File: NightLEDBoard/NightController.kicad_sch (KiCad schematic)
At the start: 10 parts

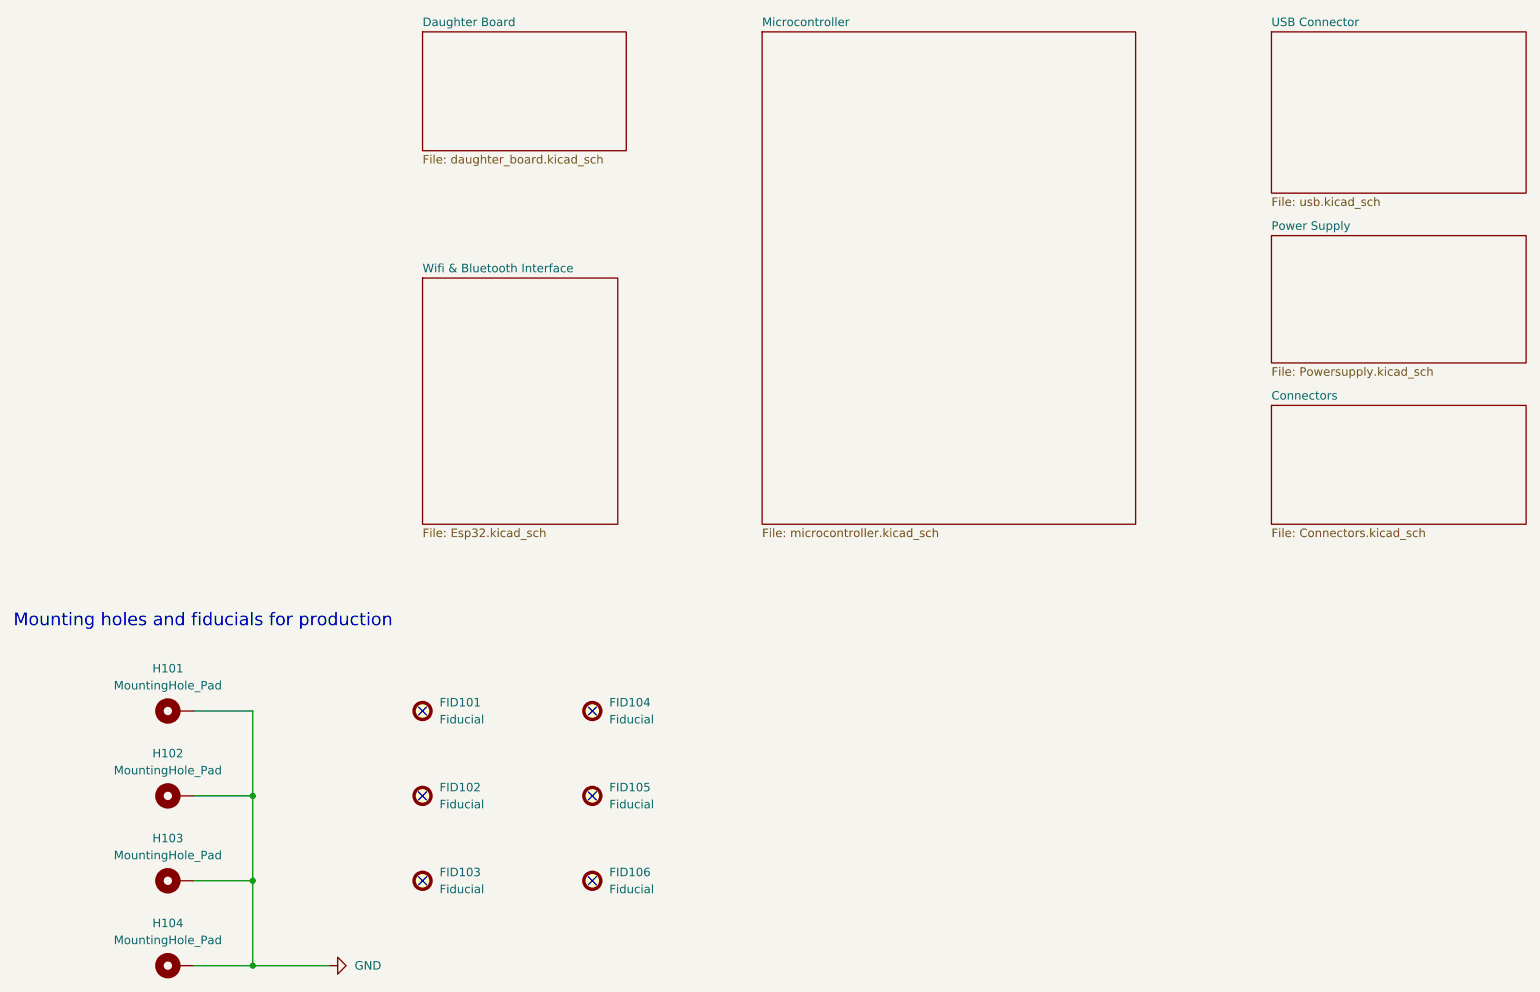
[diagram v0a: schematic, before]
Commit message: Add second pcb
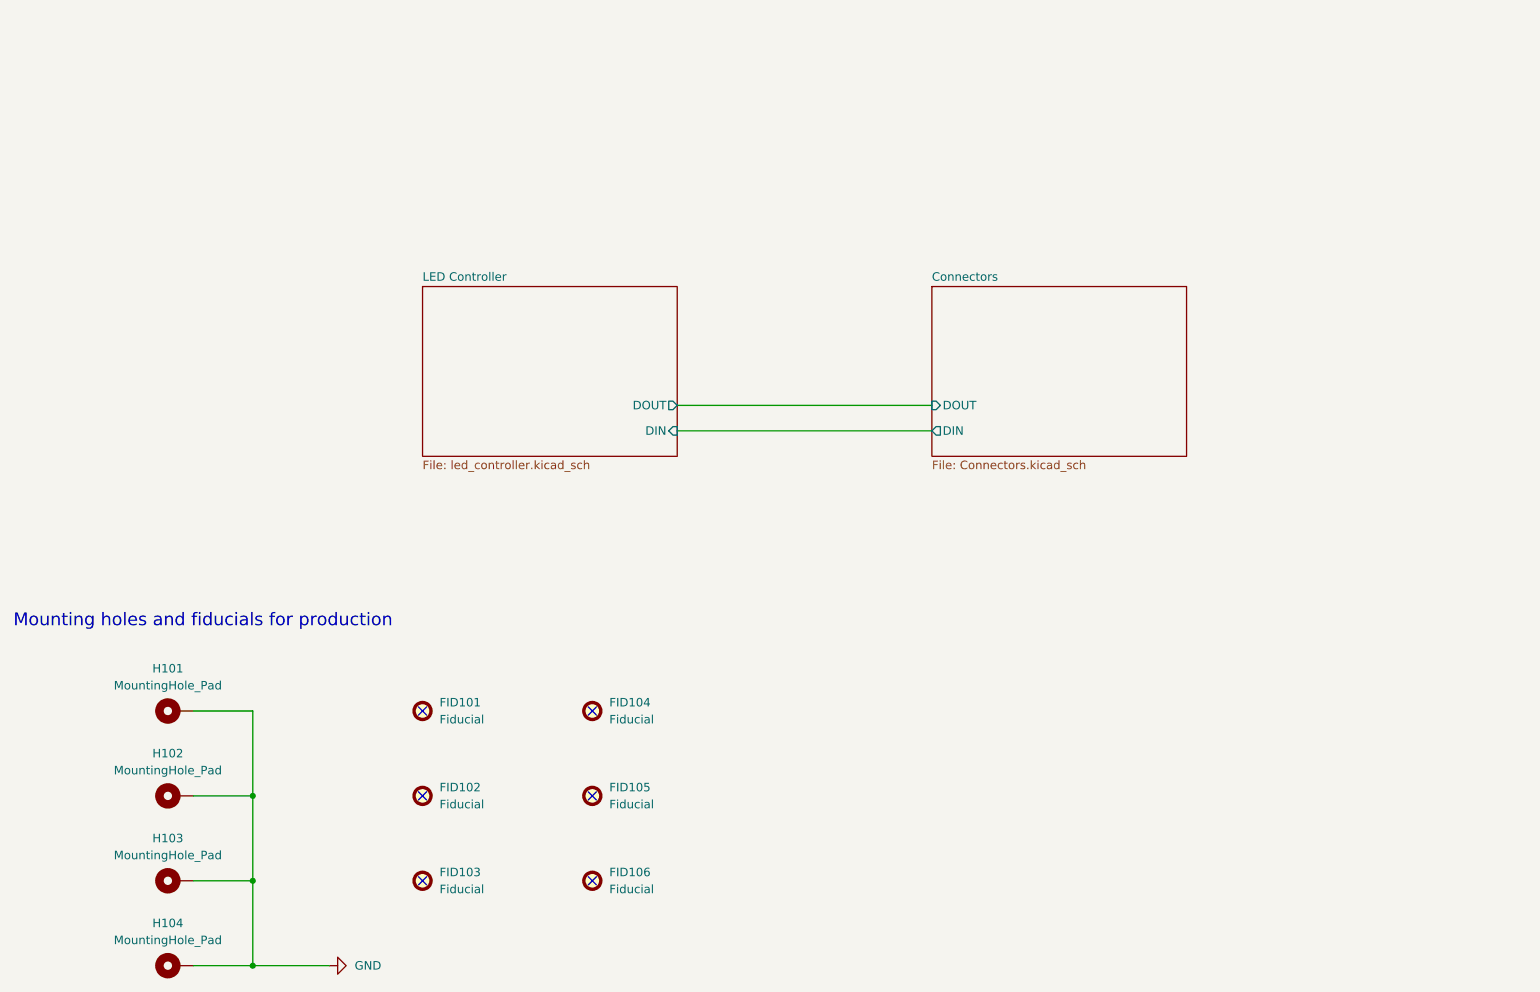
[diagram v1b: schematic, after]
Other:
- removed sheet Daughter Board
- removed sheet Microcontroller
- removed sheet Power Supply
- removed sheet USB Connector
- removed sheet Wifi & Bluetooth Interface
- added sheet LED Controller (led_controller.kicad_sch)
- sheet Connectors ports: added DIN, DOUT; removed none
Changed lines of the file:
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@@
 	(generator "eeschema")
 	(generator_version "8.0")
-	(paper "A3")
+	(paper "A4")
 	(title_block
 		(title "NightLight")
@@
 	(wire
 		(pts
+			(xy 114.3 110.49) (xy 152.4 110.49)
+		)
+		(stroke
+			(width 0)
+			(type default)
+		)
+	)
+	(wire
+		(pts
 			(xy 50.8 190.5) (xy 62.23 190.5)
 		)
@@
 		(pts
 			(xy 50.8 190.5) (xy 41.91 190.5)
+		)
+		(stroke
+			(width 0)
+			(type default)
+		)
+	)
+	(wire
+		(pts
+			(xy 114.3 106.68) (xy 152.4 106.68)
 		)
 		(stroke
@@
 	)
 	(sheet
-		(at 76.2 87.63)
-		(size 29.21 36.83)
+		(at 152.4 88.9)
+		(size 38.1 25.4)
 		(fields_autoplaced yes)
 		(stroke
@@
 			(color 0 0 0 0.0000)
 		)
-		(property "Sheetname" "Wifi & Bluetooth Interface"
-			(at 76.2 86.9184 0)
+		(property "Sheetname" "Connectors"
+			(at 152.4 88.1884 0)
 			(effects
 				(font
@@
 			)
 		)
-		(property "Sheetfile" "Esp32.kicad_sch"
-			(at 76.2 125.0446 0)
+		(property "Sheetfile" "Connectors.kicad_sch"
+			(at 152.4 114.8846 0)
 			(effects
 				(font
@@
 			)
 		)
-		(instances
-			(project "NightController"
-				(path "/84972824-c6a3-4762-8148-c4d5b5ede147"
-					(page "4")
+		(pin "DOUT" input
+			(at 152.4 106.68 180)
+			(effects
+				(font
+					(size 1.27 1.27)
+				)
+				(justify left)
+			)
+		)
+		(pin "DIN" output
+			(at 152.4 110.49 180)
+			(effects
+				(font
+					(size 1.27 1.27)
+				)
+				(justify left)
+			)
+		)
+		(instances
+			(project "NightController"
+				(path "/84972824-c6a3-4762-8148-c4d5b5ede147"
+					(page "2")
 				)
 			)
@@
 	)
 	(sheet
-		(at 76.2 50.8)
-		(size 30.48 17.78)
+		(at 76.2 88.9)
+		(size 38.1 25.4)
 		(fields_autoplaced yes)
 		(stroke
@@
 			(color 0 0 0 0.0000)
 		)
-		(property "Sheetname" "Daughter Board"
-			(at 76.2 50.0884 0)
+		(property "Sheetname" "LED Controller"
+			(at 76.2 88.1884 0)
 			(effects
 				(font
@@
 			)
 		)
-		(property "Sheetfile" "daughter_board.kicad_sch"
-			(at 76.2 69.1646 0)
+		(property "Sheetfile" "led_controller.kicad_sch"
+			(at 76.2 114.8846 0)
 			(effects
 				(font
@@
 			)
 		)
+		(pin "DIN" input
+			(at 114.3 110.49 0)
+			(effects
+				(font
+					(size 1.27 1.27)
+				)
+				(justify right)
+			)
+		)
+		(pin "DOUT" output
+			(at 114.3 106.68 0)
+			(effects
+				(font
+					(size 1.27 1.27)
+				)
+				(justify right)
+			)
+		)
 		(instances
 			(project "NightController"
@@
 				)
 			)
-		)
-	)
-	(sheet
-		(at 203.2 81.28)
-		(size 38.1 19.05)
-		(fields_autoplaced yes)
-		(stroke
-			(width 0.1524)
-			(type solid)
-		)
-		(fill
-			(color 0 0 0 0.0000)
-		)
-		(property "Sheetname" "Power Supply"
-			(at 203.2 80.5684 0)
-			(effects
-				(font
-					(size 1.27 1.27)
-				)
-				(justify left bottom)
-			)
-		)
-		(property "Sheetfile" "Powersupply.kicad_sch"
-			(at 203.2 100.9146 0)
-			(effects
-				(font
-					(size 1.27 1.27)
-				)
-				(justify left top)
-			)
-		)
-		(instances
-			(project "NightController"
-				(path "/84972824-c6a3-4762-8148-c4d5b5ede147"
-					(page "6")
-				)
-			)
-		)
-	)
-	(sheet
-		(at 203.2 106.68)
-		(size 38.1 17.78)
-		(fields_autoplaced yes)
-		(stroke
-			(width 0.1524)
-			(type solid)
-		)
-		(fill
-			(color 0 0 0 0.0000)
-		)
-		(property "Sheetname" "Connectors"
-			(at 203.2 105.9684 0)
-			(effects
-				(font
-					(size 1.27 1.27)
-				)
-				(justify left bottom)
-			)
-		)
-		(property "Sheetfile" "Connectors.kicad_sch"
-			(at 203.2 125.0446 0)
-			(effects
-				(font
-					(size 1.27 1.27)
-				)
-				(justify left top)
-			)
-		)
-		(instances
-			(project "NightController"
-				(path "/84972824-c6a3-4762-8148-c4d5b5ede147"
-					(page "7")
-				)
-			)
-		)
-	)
-	(sheet
-		(at 127 50.8)
-		(size 55.88 73.66)
-		(fields_autoplaced yes)
-		(stroke
-			(width 0.1524)
-			(type solid)
-		)
-		(fill
-			(color 0 0 0 0.0000)
-		)
-		(property "Sheetname" "Microcontroller"
-			(at 127 50.0884 0)
-			(effects
-				(font
-					(size 1.27 1.27)
-				)
-				(justify left bottom)
-			)
-		)
-		(property "Sheetfile" "microcontroller.kicad_sch"
-			(at 127 125.0446 0)
-			(effects
-				(font
-					(size 1.27 1.27)
-				)
-				(justify left top)
-			)
-		)
-		(instances
-			(project "NightController"
-				(path "/84972824-c6a3-4762-8148-c4d5b5ede147"
-					(page "2")
-				)
-			)
-		)
-	)
-	(sheet
-		(at 203.2 50.8)
-		(size 38.1 24.13)
-		(fields_autoplaced yes)
-		(stroke
-			(width 0.1524)
-			(type solid)
-		)
-		(fill
-			(color 0 0 0 0.0000)
-		)
-		(property "Sheetname" "USB Connector"
-			(at 203.2 50.0884 0)
-			(effects
-				(font
-					(size 1.27 1.27)
-				)
-				(justify left bottom)
-			)
-		)
-		(property "Sheetfile" "usb.kicad_sch"
-			(at 203.2 75.5146 0)
-			(effects
-				(font
-					(size 1.27 1.27)
-				)
-				(justify left top)
-			)
-		)
-		(instances
-			(project "NightController"
-				(path "/84972824-c6a3-4762-8148-c4d5b5ede147"
-					(page "5")
-				)
-			)
